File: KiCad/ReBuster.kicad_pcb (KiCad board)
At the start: 4 copper layers, 38 x 38 mm, 41 parts, among them U1 10M02SCU169, U2 LM1117-3.3, U3 SN74CBTD16210, U4 SN74LVC16T245DGVR, U5 SN74CBTD16210, U6 SN74CBTD16210, U7 74LVC2T45DC, U8 PLCC_84_plug, U9 PLCC_84_plug

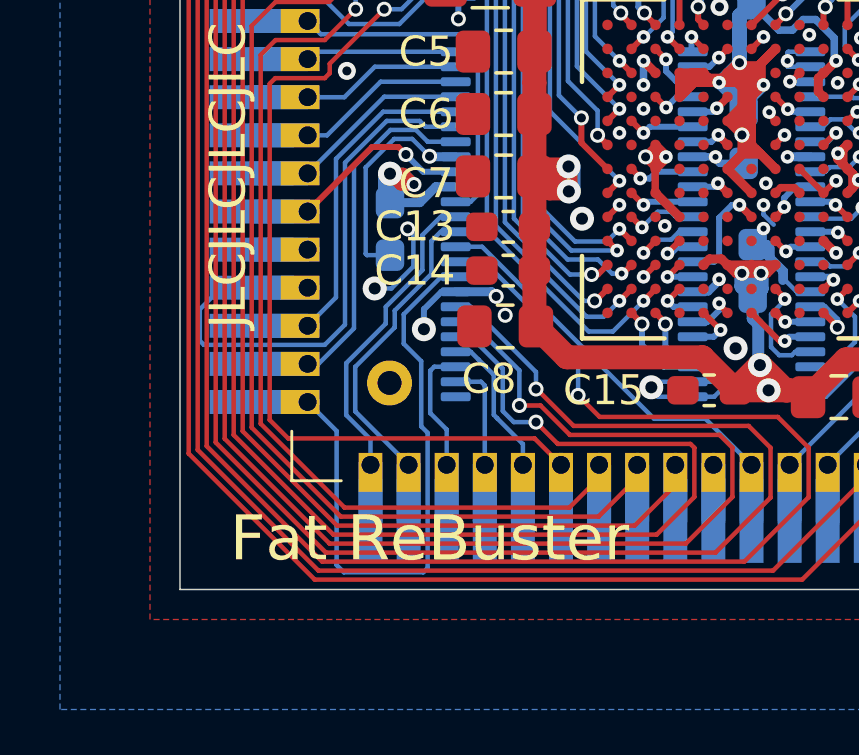
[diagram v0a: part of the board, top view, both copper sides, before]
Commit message: remove CDAC clock (not used) and put /MTCR signal there
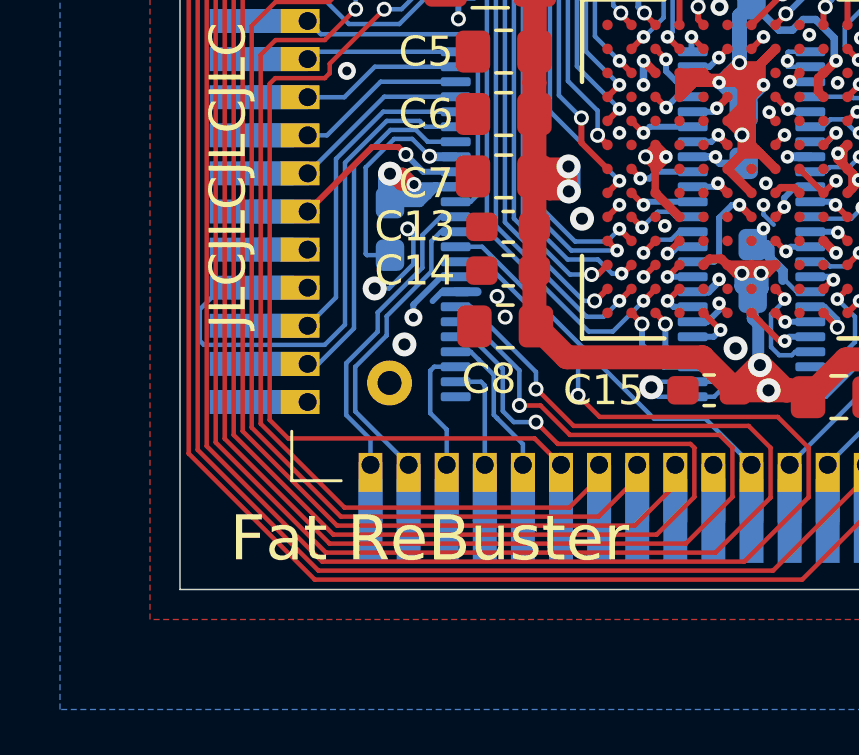
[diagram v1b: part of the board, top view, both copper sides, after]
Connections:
- net CDAC_FPGA renamed MTCR_CBTD_FPGA
- U6 pad 9: CDAC -> MTCR
- U8 pad 32: CDAC -> /CDAC
- U9 pad 32: CDAC -> /CDAC
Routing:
- net MTCR: track 64.0 -> 108.4 mm, vias 1 -> 2
- net VCC: track 90.3 -> 119.6 mm
- net CDAC: track 21.9 -> 0.00 mm
- net GND: track 69.0 -> 66.1 mm
- net /CDAC: track 0.00 -> 1.88 mm

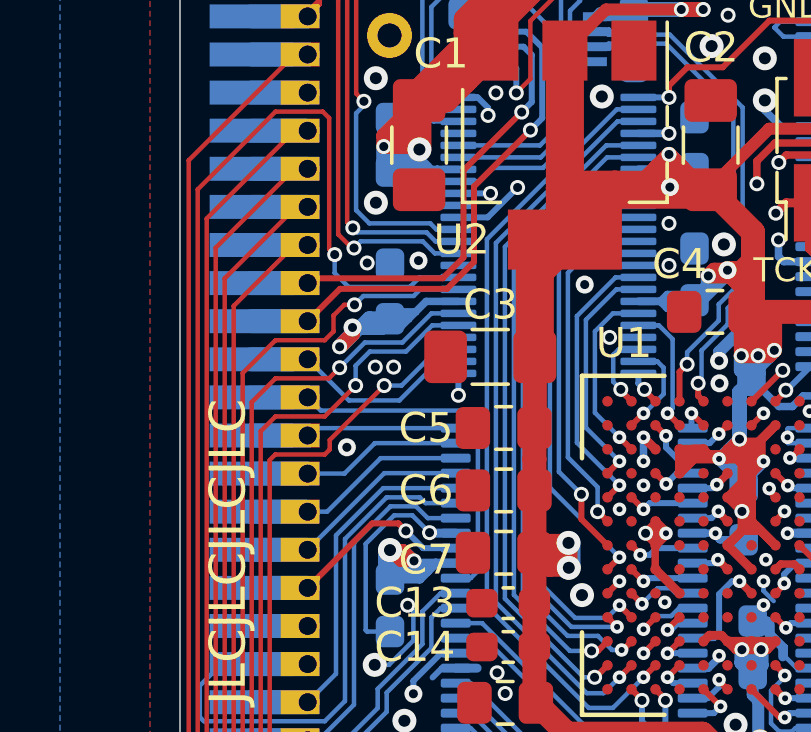
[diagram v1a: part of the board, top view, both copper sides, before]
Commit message: remove HLT-signal (not used) and put /DTACK signal there
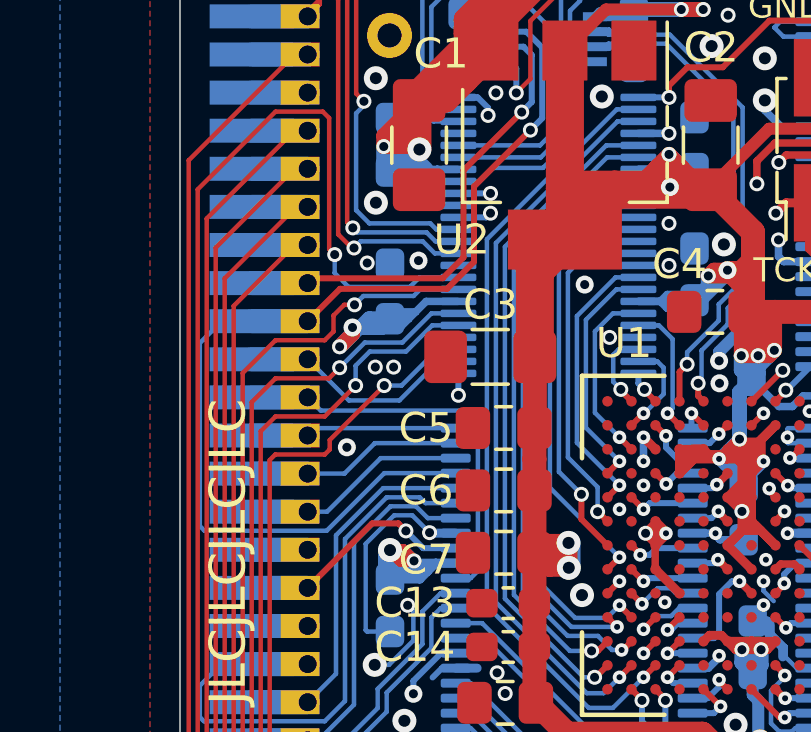
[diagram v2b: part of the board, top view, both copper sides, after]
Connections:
- net HLT_FPGA renamed DTACK_CBTD_FPGA
- U6 pad 21: HLT -> DTACK
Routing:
- net DTACK: track 17.9 -> 35.4 mm
- net HLT: track 7.86 -> 1.87 mm

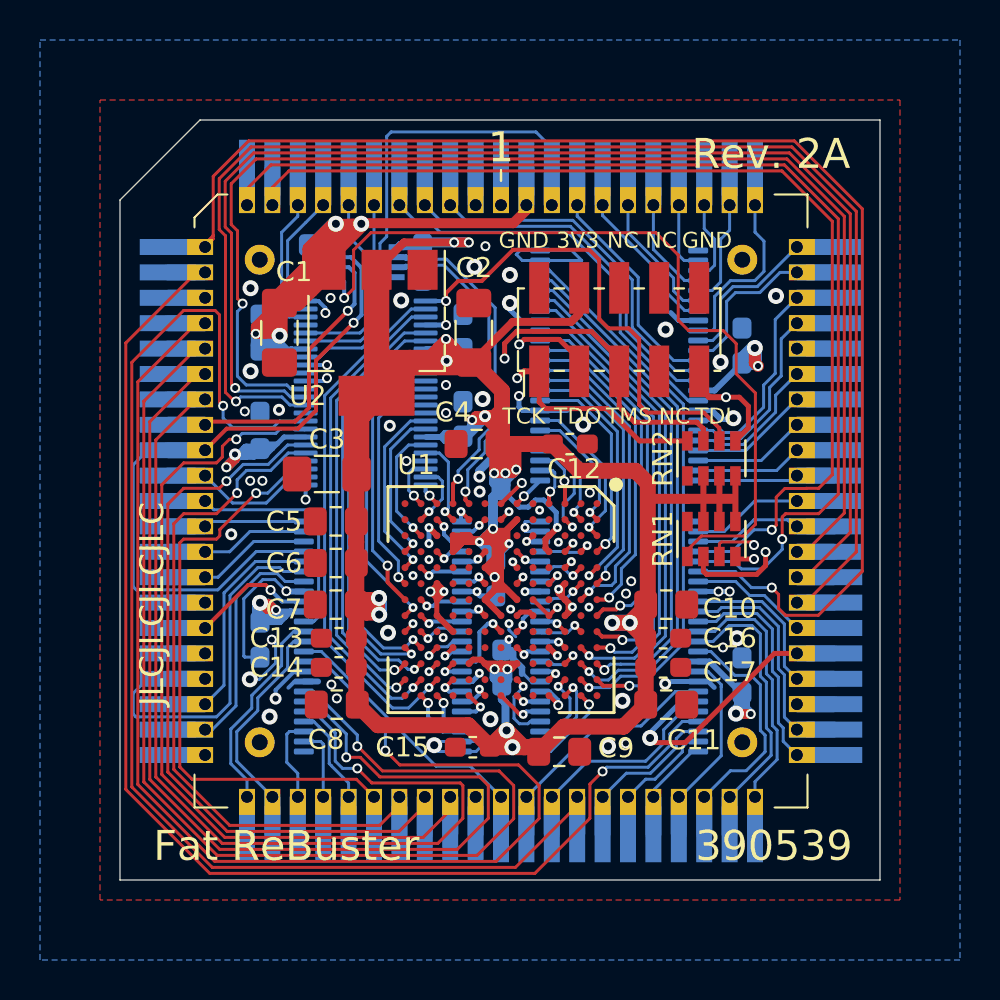
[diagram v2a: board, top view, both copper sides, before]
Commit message: Replace 74LVC2T45DC with 74LVC2G07GV and prepare rerouting, reroute /DTACK
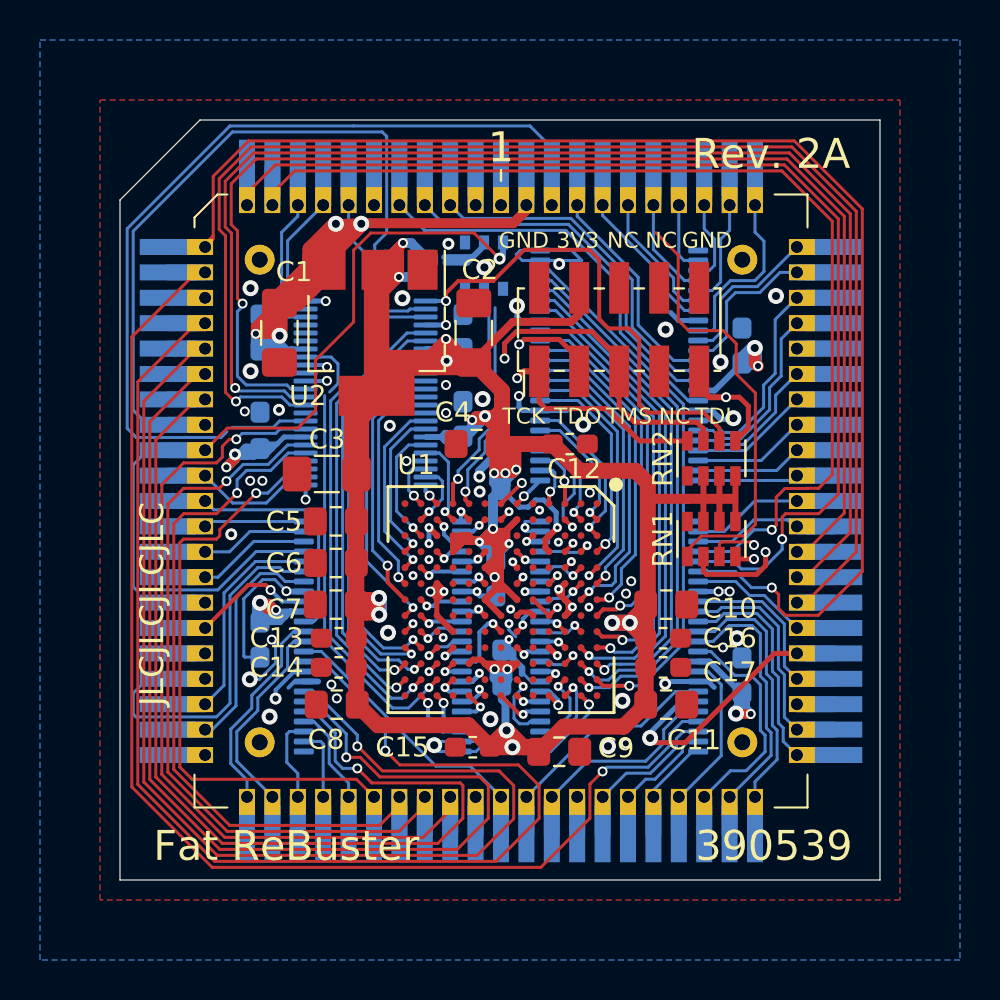
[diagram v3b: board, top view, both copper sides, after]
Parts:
- removed C26: 0.1uF, Capacitor_SMD:C_0603_1608Metric_Pad1.08x0.95mm_HandSolder
- U7: value 74LVC2T45DC -> 74LVC2G07GV,125; footprint Package_SO:VSSOP-8_2.3x2mm_P0.5mm -> Package_SO:TSOP-6_1.65x3.05mm_P0.95mm
- moved U7 5.92 mm to (143.6, 62.7), turned to 90 degrees
- moved C29 0.70 mm to (139.8, 62.4), turned to 0 degrees
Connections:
- net HLT renamed /HLT
- U7 pad 1: 3V3 -> DTACK_FPGA
- U7 pad 2: DTACK_FPGA -> GND
- U7 pad 3: MTACK_FPGA -> Net-(U7-Pad3)
- U7 pad 4: GND -> Net-(U7-Pad4)
- U7 pad 5: DIR_U7 -> 3V3
- U7 pad 6: MTACK -> DTACK
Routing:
- net MTCR: track 108.4 -> 55.8 mm
- net DIR_U7: track 63.8 -> 43.6 mm, vias 2 -> 1
- net MTACK: track 16.2 -> 36.0 mm, vias 1 -> 0
- net EDS1: track 25.6 -> 45.3 mm
- net RW: track 11.7 -> 1.87 mm
- net DTACK: track 35.4 -> 43.6 mm
- net SIZ0: track 11.5 -> 4.81 mm
- net DTACK_FPGA: track 17.6 -> 10.9 mm
- net VCC: track 119.6 -> 113.0 mm
- net MTACK_FPGA: track 17.2 -> 10.9 mm
- net 3V3: track 235.7 -> 241.3 mm
- net SIZ1_FPGA: track 26.7 -> 21.9 mm
- net GND: track 66.1 -> 62.9 mm, vias 62 -> 60
- net AS_FPGA: track 24.6 -> 21.7 mm
- net FCS: track 17.0 -> 16.0 mm
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
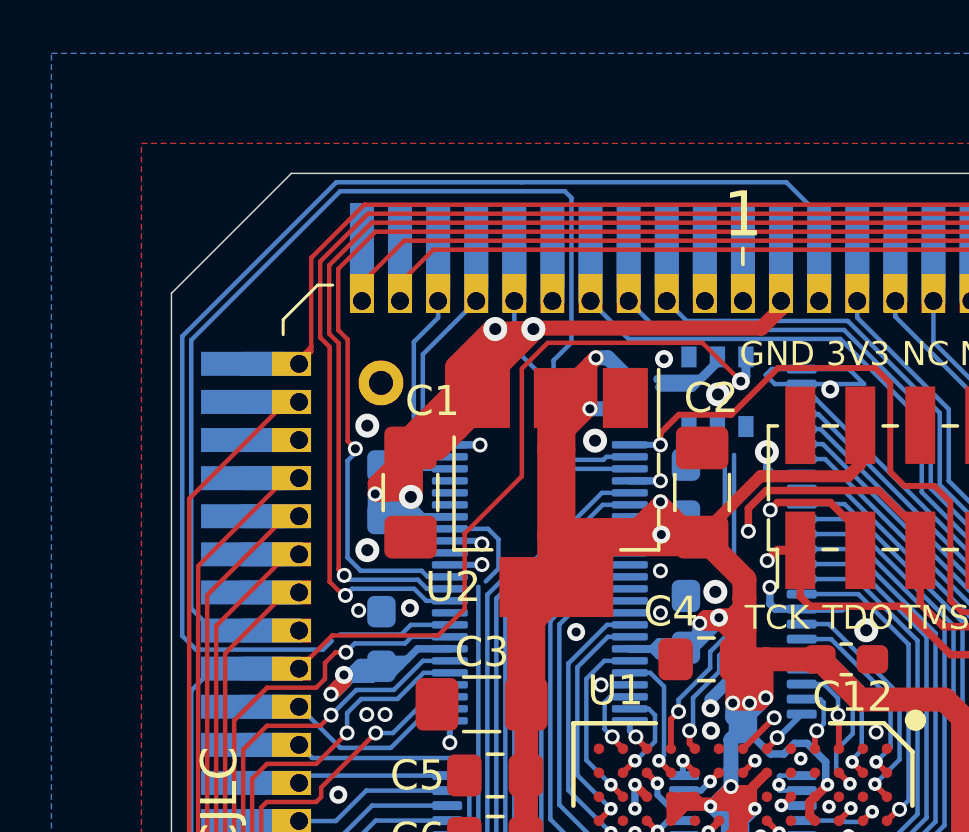
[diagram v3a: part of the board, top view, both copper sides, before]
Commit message: Relocate EDS1 signal to replace MTCR's position (pin 9 and 40) in SN74LVC16T245
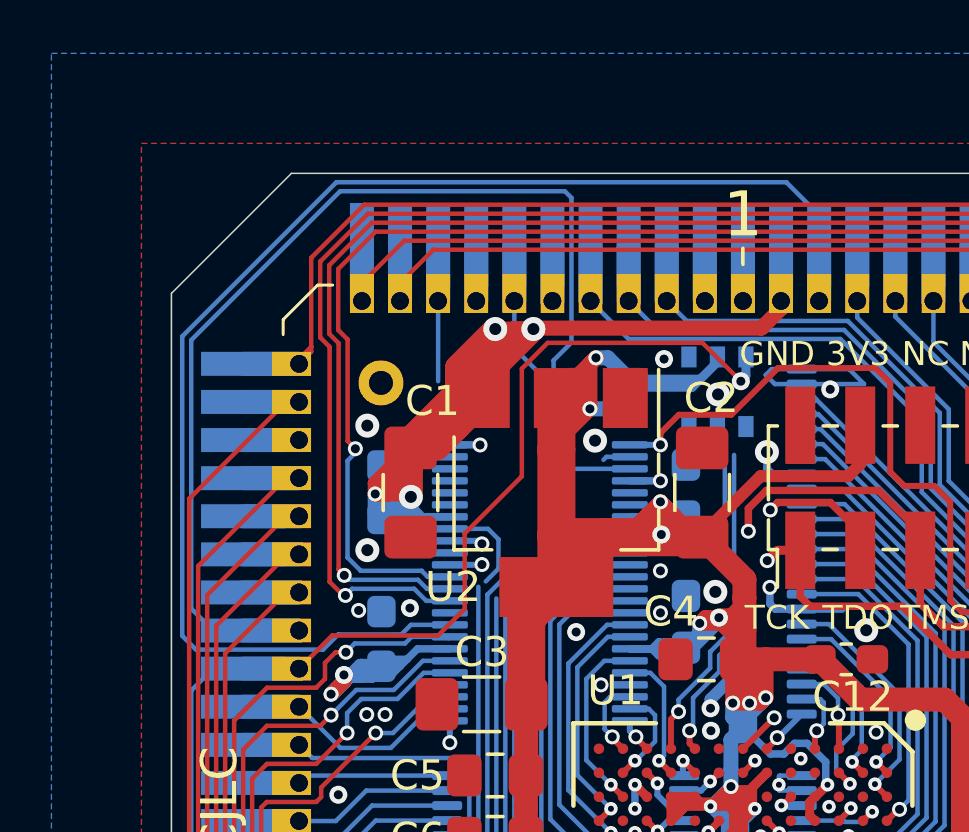
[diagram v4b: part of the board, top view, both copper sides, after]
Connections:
- U1 pad M11: EDS1_FPGA -> Net-(U1-PadM11)
- U1 pad N5: MTCR_FPGA -> EDS1_FPGA
- U4 pad 17: EDS1 -> Net-(U4-Pad17)
- U4 pad 32: EDS1_FPGA -> Net-(U4-Pad32)
- U4 pad 40: MTCR_FPGA -> EDS1_FPGA
- U4 pad 9: MTCR -> EDS1
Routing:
- net Net-(U1-PadM11): track 0.00 -> 15.6 mm, vias 0 -> 1
- net EDS1_FPGA: track 20.6 -> 9.38 mm
- net MTCR_FPGA: track 9.38 -> 0.00 mm, vias 1 -> 0
- net SIZ1: track 8.58 -> 1.87 mm
- net SIZ0_FPGA: track 22.2 -> 16.3 mm
- net RW_FPGA: track 20.9 -> 15.4 mm
- net AS: track 8.78 -> 4.54 mm
- net MTCR: track 55.8 -> 52.0 mm
- net Net-(U4-Pad17): track 0.00 -> 3.34 mm
- net 3V3: track 241.3 -> 243.2 mm
- net SIZ1_FPGA: track 21.9 -> 20.8 mm
- net EDS1: track 45.3 -> 46.1 mm

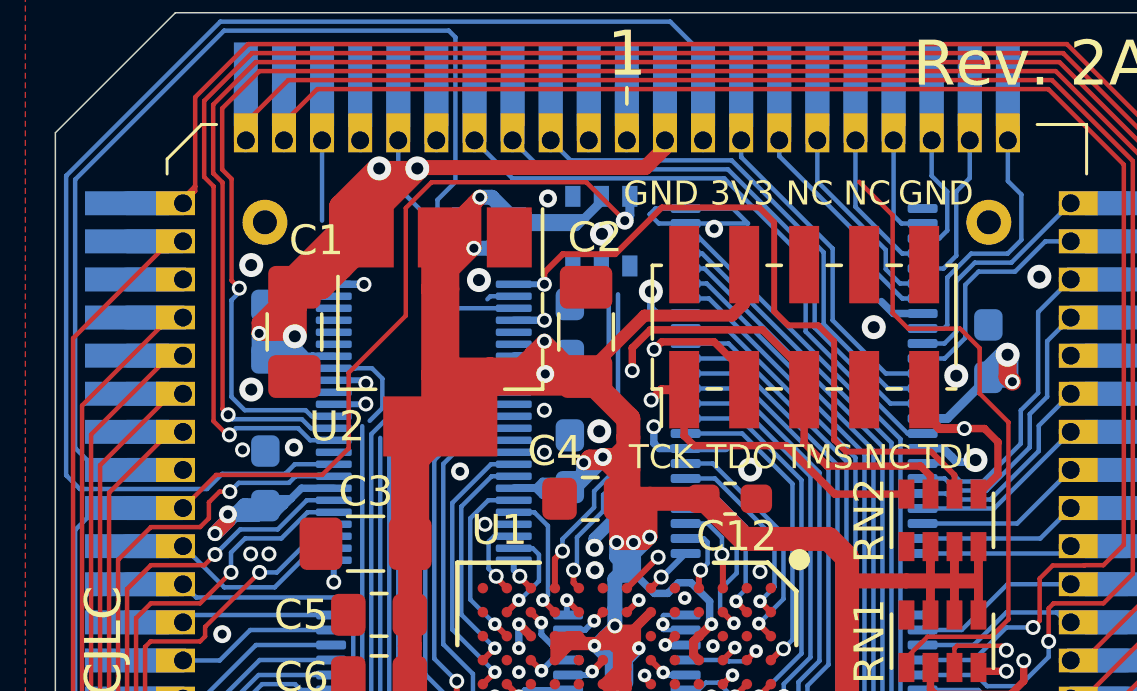
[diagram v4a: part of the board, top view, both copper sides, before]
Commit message: Replace SN74LVC16T245DGVR with SN74LVC16245ADGVR and fix caps C24,C25 to instead be connected to 3V3
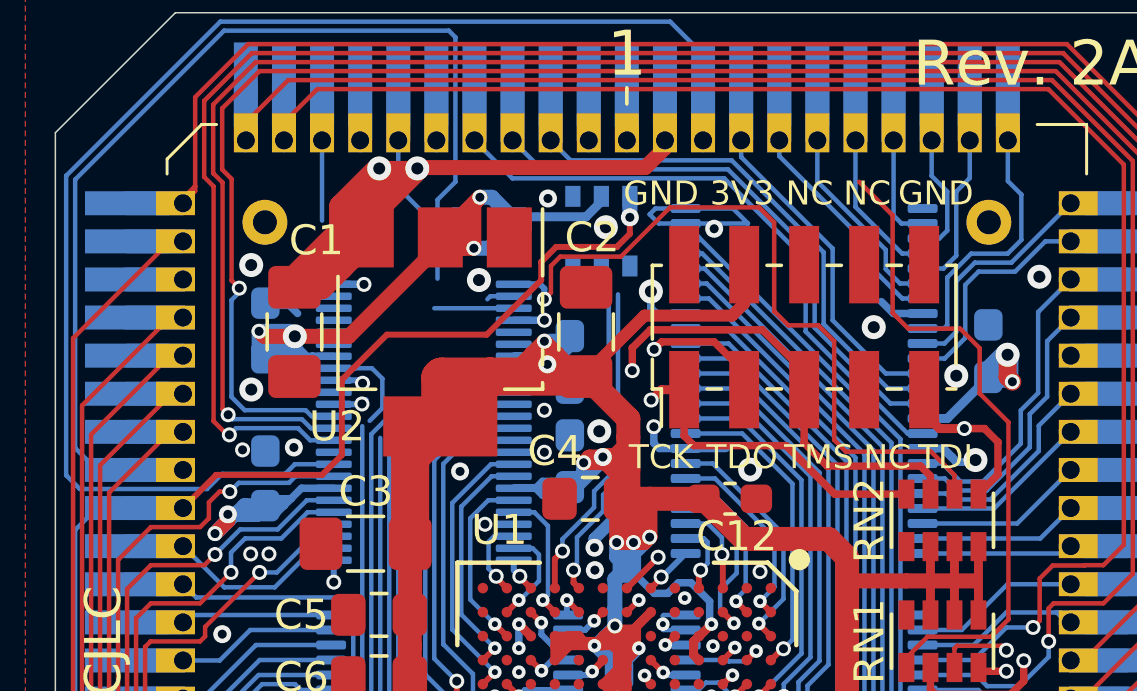
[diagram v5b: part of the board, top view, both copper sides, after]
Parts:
- C25: footprint Capacitor_SMD:C_0603_1608Metric_Pad1.05x0.95mm_HandSolder -> ReBuster:C_0603_1608Metric_Pad1.05x0.95mm_HandSolder_extended
- U4: value SN74LVC16T245DGVR -> SN74LVC16245ADGVR; footprint Package_SO:TSSOP-48_4.4x9.7mm_P0.4mm -> ReBuster:TSSOP-48_4.4x9.7mm_P0.4mm_custom
- moved C27 1.06 mm to (142.5, 67.0), turned to 90 degrees
- renumbered C27 to C26, C28 to C27, C29 to C28
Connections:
- C24 pad 2: VCC -> 3V3
- C25 pad 2: VCC -> 3V3
- U4 pad 18: VCC -> 3V3
- U4 pad 7: VCC -> 3V3
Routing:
- net VCC: track 113.0 -> 83.6 mm, vias 12 -> 8
- net 3V3: track 243.2 -> 263.5 mm, vias 27 -> 31
- net DIR_U7: track 43.6 -> 29.1 mm
- net FCS: track 16.0 -> 5.63 mm
- net DTACK: track 43.6 -> 41.1 mm
- net OE_U4: track 35.2 -> 35.8 mm
